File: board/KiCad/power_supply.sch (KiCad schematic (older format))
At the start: 8 parts, among them CON1 BARREL_JACK, Q1 IRLML6344bpf, U2 LD6815

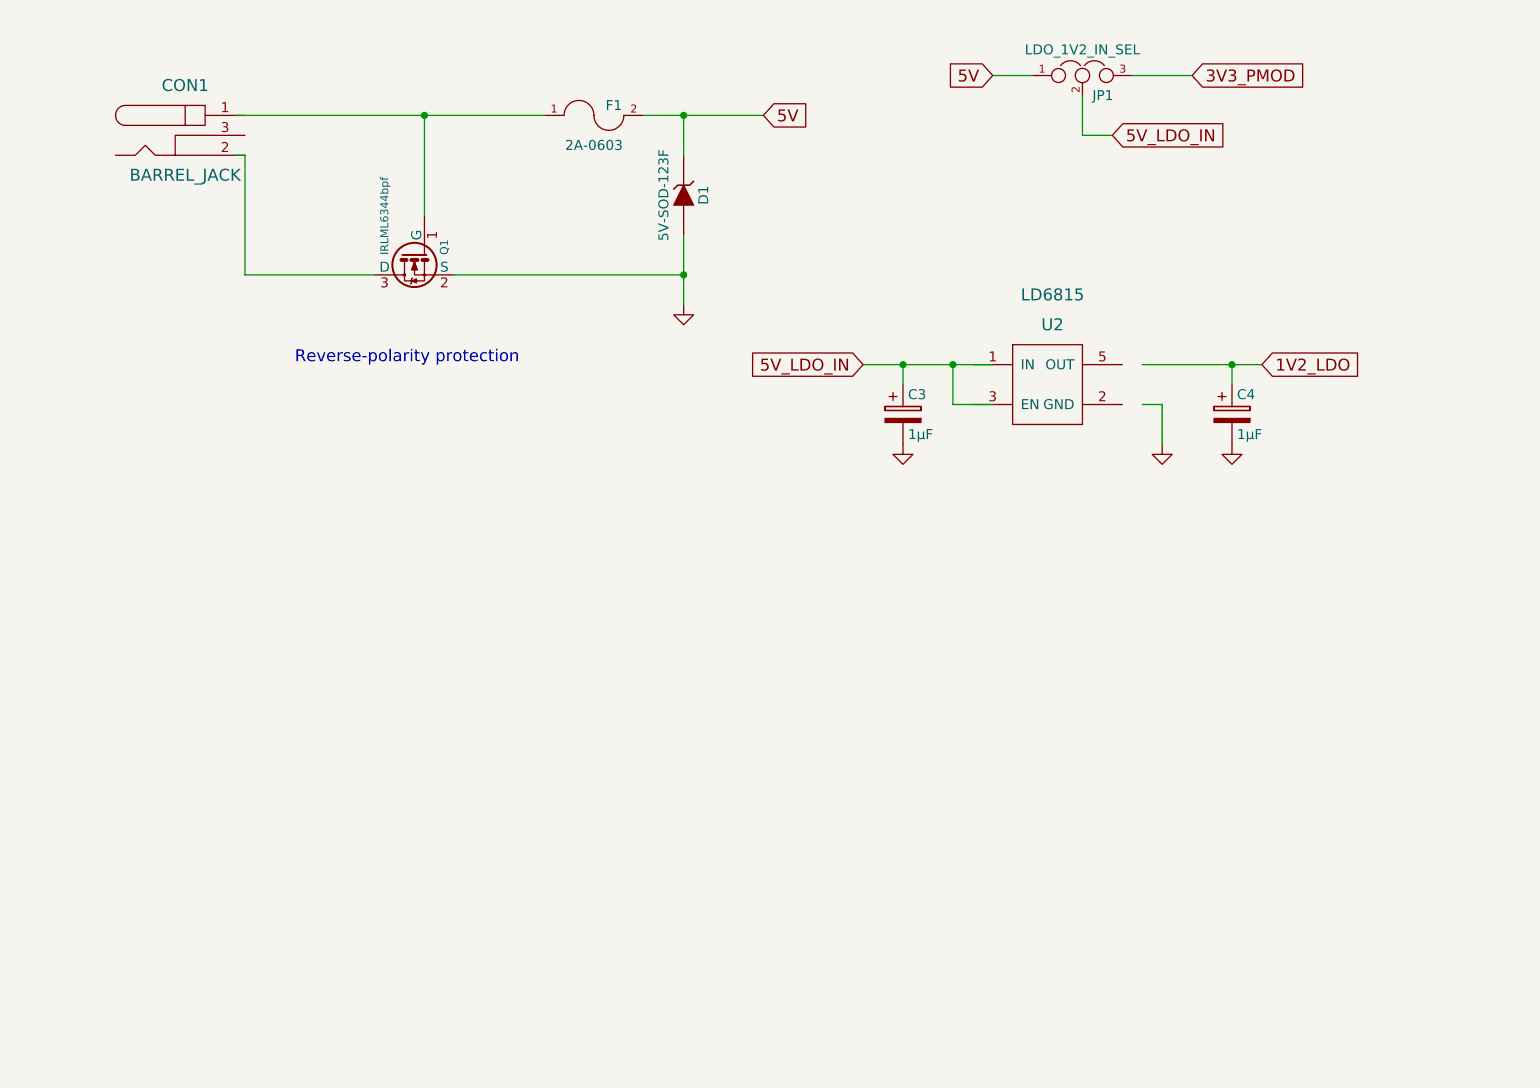
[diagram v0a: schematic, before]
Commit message: added annotations
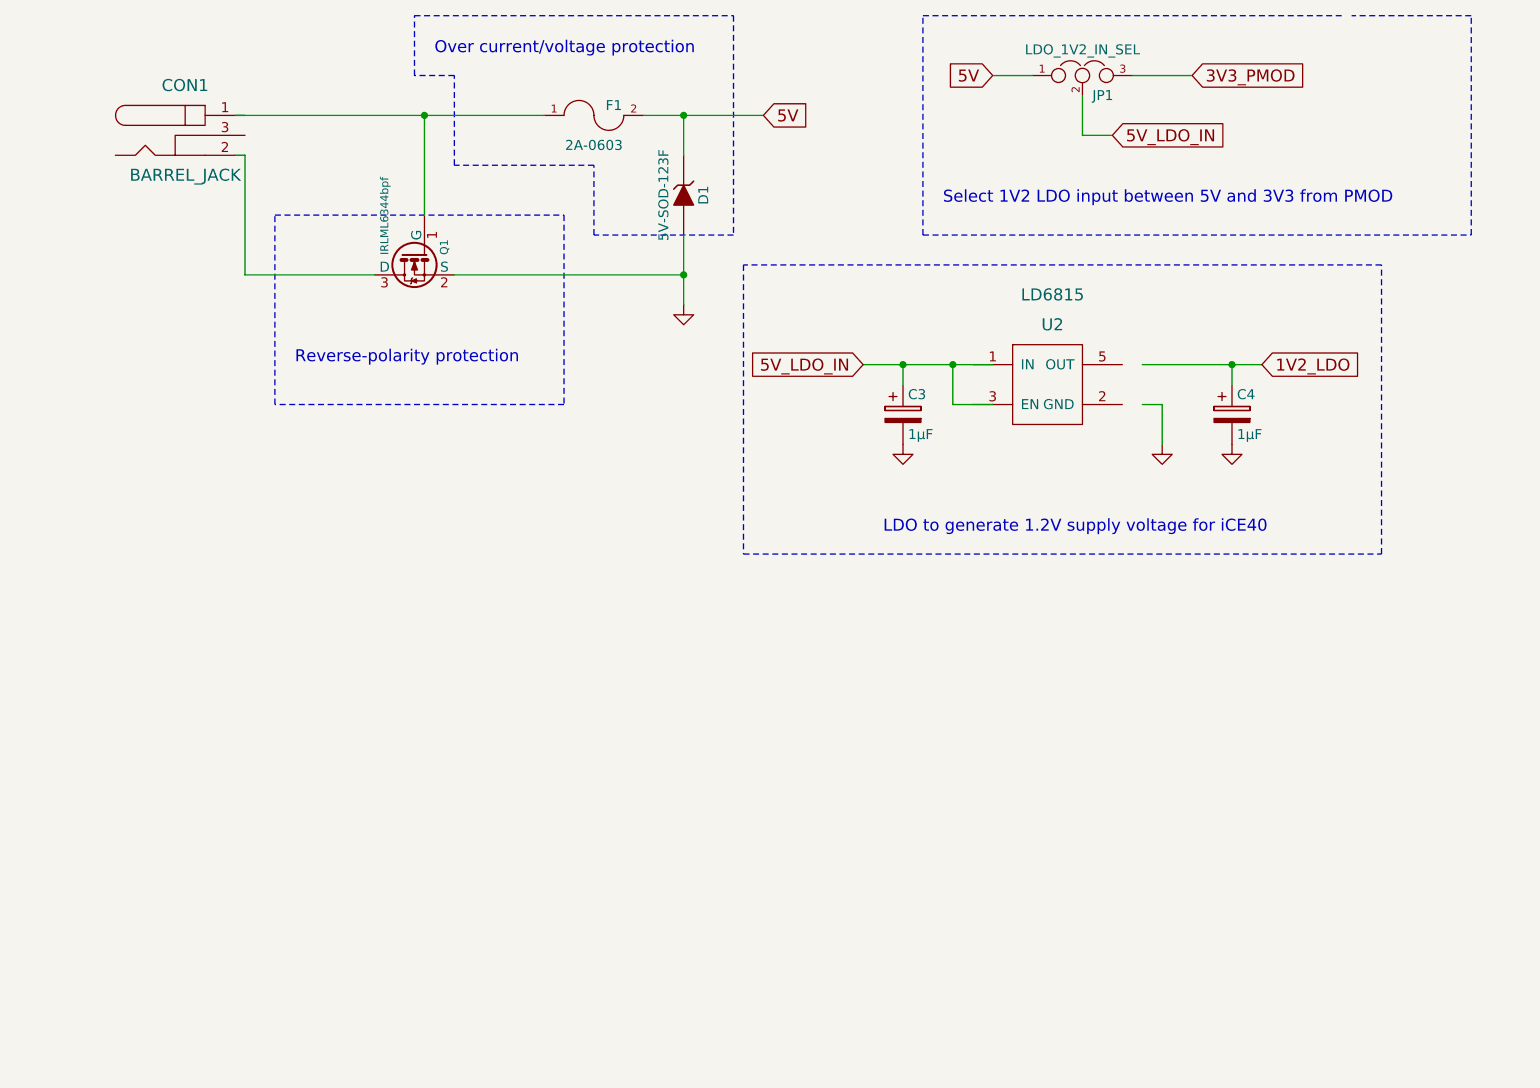
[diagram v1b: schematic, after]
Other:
- note added: "LDO to generate 1.2V supply voltage for iCE40"
- note added: "Over current/voltage protection"
- note added: "Select 1V2 LDO input between 5V and 3V3 from PMOD"
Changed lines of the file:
@@
 	4600 2300 4600 2650
 Connection ~ 4600 2500
+Wire Notes Line
+	2550 3150 2550 2200
+Wire Notes Line
+	2550 2200 4000 2200
+Wire Notes Line
+	4000 2200 4000 3150
+Wire Notes Line
+	4000 3150 2550 3150
+Text Notes 3350 1400 0    60   ~ 0
+Over current/voltage protection
+Wire Notes Line
+	3250 1200 4850 1200
+Wire Notes Line
+	4850 1200 4850 2300
+Wire Notes Line
+	4850 2300 4150 2300
+Wire Notes Line
+	4150 2300 4150 1950
+Wire Notes Line
+	4150 1950 3450 1950
+Wire Notes Line
+	3450 1950 3450 1500
+Wire Notes Line
+	3450 1500 3250 1500
+Wire Notes Line
+	3250 1500 3250 1200
+Wire Notes Line
+	5800 1200 7900 1200
+Wire Notes Line
+	5800 2300 8550 2300
+Wire Notes Line
+	5800 2300 5800 1200
+Text Notes 5900 2150 0    60   ~ 0
+Select 1V2 LDO input between 5V and 3V3 from PMOD
+Wire Notes Line
+	8550 2300 8550 1200
+Wire Notes Line
+	8550 1200 7950 1200
+Text Notes 5600 3800 0    60   ~ 0
+LDO to generate 1.2V supply voltage for iCE40
+Wire Notes Line
+	4900 2450 4900 3900
+Wire Notes Line
+	4900 3900 8100 3900
+Wire Notes Line
+	8100 3900 8100 2450
+Wire Notes Line
+	8100 2450 4900 2450
 $EndSCHEMATC

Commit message: SPI & Osci
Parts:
- added C?: 0.1µ, symbol C
- added J?: SELECT_DIV, Pinhead_1x3_TH, symbol Pinheader_1x3_TH
- added R?: R, symbol R
- added U?: LTC1799, symbol LTC1799
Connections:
- net labels added: ICE_CLK_IN
- wire segments 21 -> 34
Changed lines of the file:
@@
 $Descr A4 11693 8268
 encoding utf-8
-Sheet 5 5
+Sheet 5 6
 Title ""
 Date ""
@@
 Wire Notes Line
 	8100 2450 4900 2450
+$Comp
+L LTC1799 U?
+U 1 1 56BD2D04
+P 3450 6100
+F 0 "U?" H 3450 6100 60  0000 C CNN
+F 1 "LTC1799" H 3450 7100 60  0000 C CNN
+F 2 "" H 3450 6100 60  0000 C CNN
+F 3 "" H 3450 6100 60  0000 C CNN
+	1    3450 6100
+	1    0    0    -1
+$EndComp
+Text GLabel 2000 5350 0    60   Input ~ 0
+3V3_PMOD
+$Comp
+L C C?
+U 1 1 56BD346E
+P 2200 5600
+F 0 "C?" H 2225 5700 50  0000 L CNN
+F 1 "0.1µ" H 2225 5500 50  0000 L CNN
+F 2 "" H 2238 5450 30  0000 C CNN
+F 3 "" H 2200 5600 60  0000 C CNN
+	1    2200 5600
+	1    0    0    -1
+$EndComp
+$Comp
+L GND #PWR?
+U 1 1 56BD34C1
+P 2200 6100
+F 0 "#PWR?" H 2200 5850 50  0001 C CNN
+F 1 "GND" H 2200 5950 50  0000 C CNN
+F 2 "" H 2200 6100 60  0000 C CNN
+F 3 "" H 2200 6100 60  0000 C CNN
+	1    2200 6100
+	1    0    0    -1
+$EndComp
+Wire Wire Line
+	2000 5350 3000 5350
+Wire Wire Line
+	2200 5450 2200 5350
+Connection ~ 2200 5350
+Wire Wire Line
+	2200 5750 2200 6100
+$Comp
+L R R?
+U 1 1 56BD37E8
+P 2650 5600
+F 0 "R?" V 2730 5600 50  0000 C CNN
+F 1 "R" V 2650 5600 50  0000 C CNN
+F 2 "" V 2580 5600 30  0000 C CNN
+F 3 "" H 2650 5600 30  0000 C CNN
+	1    2650 5600
+	0    1    1    0
+$EndComp
+Wire Wire Line
+	2800 5600 3000 5600
+Wire Wire Line
+	2500 5350 2500 5600
+Connection ~ 2500 5350
+Wire Wire Line
+	3000 5850 2200 5850
+Connection ~ 2200 5850
+$Comp
+L Pinheader_1x3_TH J?
+U 1 1 56BD3EF9
+P 4400 5800
+F 0 "J?" H 4400 6050 60  0000 C CNN
+F 1 "SELECT_DIV" H 4400 6190 60  0001 C CNN
+F 2 "Pinhead_1x3_TH" H 4390 6300 60  0001 C CNN
+F 3 "" H 4400 5800 60  0000 C CNN
+F 4 "609-3461-ND" H 4380 6820 60  0001 C CNN "Vendor Part Number"
+F 5 "68000-103HLF" H 4370 6530 60  0001 C CNN "Manufacturer Part Number"
+F 6 "BERGSTIK II, .100\", SR, STRAIGHT," H 4350 6410 60  0001 C CNN "Description"
+F 7 "Digi-Key" H 4370 6730 60  0001 C CNN "Vendor"
+F 8 "FCI" H 4360 6620 60  0001 C CNN "Manufacturer"
+F 9 "PinH_1x3_TH" H 4410 5650 60  0000 C CNN "Component Value"
+	1    4400 5800
+	-1   0    0    1
+$EndComp
+Wire Wire Line
+	3900 5850 4150 5850
+$Comp
+L GND #PWR?
+U 1 1 56BD3FC7
+P 4100 6050
+F 0 "#PWR?" H 4100 5800 50  0001 C CNN
+F 1 "GND" H 4100 5900 50  0000 C CNN
+F 2 "" H 4100 6050 60  0000 C CNN
+F 3 "" H 4100 6050 60  0000 C CNN
+	1    4100 6050
+	1    0    0    -1
+$EndComp
+Wire Wire Line
+	4100 6050 4100 5950
+Wire Wire Line
+	4100 5950 4150 5950
+Text GLabel 4250 5550 2    60   Input ~ 0
+3V3_PMOD
+Wire Wire Line
+	4150 5750 4000 5750
+Wire Wire Line
+	4000 5750 4000 5550
+Wire Wire Line
+	4000 5550 4250 5550
+Text GLabel 4250 5350 2    60   Input ~ 0
+ICE_CLK_IN
+Wire Wire Line
+	3900 5350 4250 5350
 $EndSCHEMATC

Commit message: minor changes
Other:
- note added: "Clock generation"
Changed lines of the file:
@@
 $EndComp
 Text GLabel 2000 5350 0    60   Input ~ 0
-3V3_PMOD
+5V_LDO_IN
 $Comp
 L C C?
@@
 	4100 5950 4150 5950
 Text GLabel 4250 5550 2    60   Input ~ 0
-3V3_PMOD
+5V_LDO_IN
 Wire Wire Line
 	4150 5750 4000 5750
@@
 Wire Wire Line
 	3900 5350 4250 5350
+Wire Notes Line
+	1250 4900 5100 4900
+Wire Notes Line
+	5100 4900 5100 6500
+Wire Notes Line
+	5100 6500 1250 6500
+Wire Notes Line
+	1250 6500 1250 4900
+Text Notes 2750 6400 0    60   ~ 0
+Clock generation
 $EndSCHEMATC

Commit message: Finalize first draft
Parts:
- C3, C4: footprint (none) -> Capacitors_Tantalum_SMD:TantalC_SizeA_EIA-3216_HandSoldering
- C5: renamed from C?; footprint (none) -> Capacitors_SMD:C_0603_HandSoldering
- CON1: footprint (none) -> Connect:BARREL_JACK
- D1: footprint (none) -> pmod:SOD-123F_Handsoldering
- F1: footprint (none) -> Capacitors_SMD:C_0603_HandSoldering
- J3: renamed from J?; footprint Pinhead_1x3_TH -> Pin_Headers:Pin_Header_Straight_1x03
- JP1: footprint (none) -> Pin_Headers:Pin_Header_Straight_1x03
- Q1: footprint (none) -> TO_SOT_Packages_SMD:SOT-23_Handsoldering
- R5: renamed from R?; footprint (none) -> Resistors_SMD:R_0603_HandSoldering
- U2: footprint (none) -> pmod:SOT-753_(TSOP-5)_Handsoldering
- U3: renamed from U?; footprint (none) -> pmod:TSOT-23_Handsoldering
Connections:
- wire segments 34 -> 35
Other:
- moved on the sheet: U2
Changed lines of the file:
@@
 F 0 "Q1" H 3250 2251 40  0000 R CNN
 F 1 "IRLML6344bpf" H 3250 2550 40  0000 R CNN
-F 2 "" H 3120 2502 29  0000 C CNN
+F 2 "TO_SOT_Packages_SMD:SOT-23_Handsoldering" H 3120 2502 29  0001 C CNN
 F 3 "" H 3250 2400 60  0000 C CNN
 	1    3250 2400
@@
 $EndComp
 Wire Wire Line
-	2350 1700 3900 1700
-Wire Wire Line
 	3300 1700 3300 2200
-Wire Wire Line
-	2350 1900 2400 1900
-Wire Wire Line
-	2400 1900 2400 2500
-Wire Wire Line
-	2400 2500 3050 2500
 Wire Wire Line
 	3450 2500 4600 2500
 Connection ~ 3300 1700
 $Comp
-L GND #PWR14
+L GND #PWR15
 U 1 1 56A748C9
 P 4600 2650
-F 0 "#PWR14" H 4600 2650 30  0001 C CNN
+F 0 "#PWR15" H 4600 2650 30  0001 C CNN
 F 1 "GND" H 4600 2580 30  0001 C CNN
 F 2 "" H 4600 2650 60  0000 C CNN
@@
 F 0 "CON1" H 2100 2050 60  0000 C CNN
 F 1 "BARREL_JACK" H 2100 1600 60  0000 C CNN
-F 2 "" H 2100 1800 60  0001 C CNN
+F 2 "Connect:BARREL_JACK" H 2100 1800 60  0001 C CNN
 F 3 "" H 2100 1800 60  0000 C CNN
 	1    2100 1800
@@
 L LD6815 U2
 U 1 1 56AB720B
-P 6450 2750
-F 0 "U2" H 6450 2750 60  0000 C CNN
-F 1 "LD6815" H 6450 2900 60  0000 C CNN
-F 2 "" H 6450 2750 60  0001 C CNN
-F 3 "" H 6450 2750 60  0000 C CNN
-	1    6450 2750
+P 6550 2750
+F 0 "U2" H 6550 2750 60  0000 C CNN
+F 1 "LD6815" H 6550 2900 60  0000 C CNN
+F 2 "pmod:SOT-753_(TSOP-5)_Handsoldering" H 6550 2750 60  0001 C CNN
+F 3 "" H 6550 2750 60  0000 C CNN
+	1    6550 2750
 	1    0    0    -1
 $EndComp
@@
 	6900 2950 7500 2950
 $Comp
-L GND #PWR16
+L GND #PWR27
 U 1 1 56AB761D
 P 7000 3350
-F 0 "#PWR16" H 7000 3350 30  0001 C CNN
+F 0 "#PWR27" H 7000 3350 30  0001 C CNN
 F 1 "GND" H 7000 3280 30  0001 C CNN
 F 2 "" H 7000 3350 60  0000 C CNN
@@
 F 0 "JP1" H 6650 1400 50  0000 L CNN
 F 1 "LDO_1V2_IN_SEL" H 6600 1600 50  0000 C BNN
-F 2 "" H 6600 1500 60  0001 C CNN
+F 2 "Pin_Headers:Pin_Header_Straight_1x03" H 6600 1500 60  0001 C CNN
 F 3 "" H 6600 1500 60  0000 C CNN
 	1    6600 1500
@@
 F 0 "C4" H 7375 3300 50  0000 L CNN
 F 1 "1µF" H 7375 3100 50  0000 L CNN
-F 2 "" H 7388 3050 30  0001 C CNN
+F 2 "Capacitors_Tantalum_SMD:TantalC_SizeA_EIA-3216_HandSoldering" H 7388 3050 30  0001 C CNN
 F 3 "" H 7350 3200 60  0000 C CNN
 	1    7350 3200
@@
 F 0 "C3" H 5725 3300 50  0000 L CNN
 F 1 "1µF" H 5725 3100 50  0000 L CNN
-F 2 "" H 5738 3050 30  0001 C CNN
+F 2 "Capacitors_Tantalum_SMD:TantalC_SizeA_EIA-3216_HandSoldering" H 5738 3050 30  0001 C CNN
 F 3 "" H 5700 3200 60  0000 C CNN
 	1    5700 3200
@@
 Connection ~ 7350 2950
 $Comp
-L GND #PWR17
+L GND #PWR29
 U 1 1 56AB861C
 P 7350 3350
-F 0 "#PWR17" H 7350 3350 30  0001 C CNN
+F 0 "#PWR29" H 7350 3350 30  0001 C CNN
 F 1 "GND" H 7350 3280 30  0001 C CNN
 F 2 "" H 7350 3350 60  0000 C CNN
@@
 $EndComp
 $Comp
-L GND #PWR15
+L GND #PWR24
 U 1 1 56AB8639
 P 5700 3350
-F 0 "#PWR15" H 5700 3350 30  0001 C CNN
+F 0 "#PWR24" H 5700 3350 30  0001 C CNN
 F 1 "GND" H 5700 3280 30  0001 C CNN
 F 2 "" H 5700 3350 60  0000 C CNN
@@
 F 0 "F1" H 4250 1750 50  0000 C CNN
 F 1 "2A-0603" H 4150 1550 50  0000 C CNN
-F 2 "" H 4150 1700 50  0001 C CNN
+F 2 "Capacitors_SMD:C_0603_HandSoldering" H 4150 1700 50  0001 C CNN
 F 3 "" H 4150 1700 50  0000 C CNN
 	1    4150 1700
@@
 F 0 "D1" H 4600 2200 50  0000 C CNN
 F 1 "5V-SOD-123F" H 4600 2000 50  0000 C CNN
-F 2 "" H 4600 2100 50  0001 C CNN
+F 2 "pmod:SOD-123F_Handsoldering" H 4600 2100 50  0001 C CNN
 F 3 "" H 4600 2100 50  0000 C CNN
 	1    4600 2100
@@
 	8100 2450 4900 2450
 $Comp
-L LTC1799 U?
+L LTC1799 U3
 U 1 1 56BD2D04
 P 3450 6100
-F 0 "U?" H 3450 6100 60  0000 C CNN
+F 0 "U3" H 3450 6100 60  0000 C CNN
 F 1 "LTC1799" H 3450 7100 60  0000 C CNN
-F 2 "" H 3450 6100 60  0000 C CNN
+F 2 "pmod:TSOT-23_Handsoldering" H 3450 6100 60  0001 C CNN
 F 3 "" H 3450 6100 60  0000 C CNN
 	1    3450 6100
@@
 5V_LDO_IN
 $Comp
-L C C?
+L C C5
 U 1 1 56BD346E
 P 2200 5600
-F 0 "C?" H 2225 5700 50  0000 L CNN
+F 0 "C5" H 2225 5700 50  0000 L CNN
 F 1 "0.1µ" H 2225 5500 50  0000 L CNN
-F 2 "" H 2238 5450 30  0000 C CNN
+F 2 "Capacitors_SMD:C_0603_HandSoldering" H 2238 5450 30  0001 C CNN
 F 3 "" H 2200 5600 60  0000 C CNN
 	1    2200 5600
@@
 $EndComp
 $Comp
-L GND #PWR?
+L GND #PWR3
 U 1 1 56BD34C1
 P 2200 6100
-F 0 "#PWR?" H 2200 5850 50  0001 C CNN
+F 0 "#PWR3" H 2200 5850 50  0001 C CNN
 F 1 "GND" H 2200 5950 50  0000 C CNN
 F 2 "" H 2200 6100 60  0000 C CNN
@@
 	2200 5750 2200 6100
 $Comp
-L R R?
+L R R5
 U 1 1 56BD37E8
 P 2650 5600
-F 0 "R?" V 2730 5600 50  0000 C CNN
+F 0 "R5" V 2730 5600 50  0000 C CNN
 F 1 "R" V 2650 5600 50  0000 C CNN
-F 2 "" V 2580 5600 30  0000 C CNN
+F 2 "Resistors_SMD:R_0603_HandSoldering" V 2580 5600 30  0001 C CNN
 F 3 "" H 2650 5600 30  0000 C CNN
 	1    2650 5600
@@
 Connection ~ 2200 5850
 $Comp
-L Pinheader_1x3_TH J?
+L Pinheader_1x3_TH J3
 U 1 1 56BD3EF9
 P 4400 5800
-F 0 "J?" H 4400 6050 60  0000 C CNN
+F 0 "J3" H 4400 6050 60  0000 C CNN
 F 1 "SELECT_DIV" H 4400 6190 60  0001 C CNN
-F 2 "Pinhead_1x3_TH" H 4390 6300 60  0001 C CNN
+F 2 "Pin_Headers:Pin_Header_Straight_1x03" H 4390 6300 60  0001 C CNN
 F 3 "" H 4400 5800 60  0000 C CNN
 F 4 "609-3461-ND" H 4380 6820 60  0001 C CNN "Vendor Part Number"
@@
 	3900 5850 4150 5850
 $Comp
-L GND #PWR?
+L GND #PWR12
 U 1 1 56BD3FC7
 P 4100 6050
-F 0 "#PWR?" H 4100 5800 50  0001 C CNN
+F 0 "#PWR12" H 4100 5800 50  0001 C CNN
 F 1 "GND" H 4100 5900 50  0000 C CNN
 F 2 "" H 4100 6050 60  0000 C CNN
@@
 Text Notes 2750 6400 0    60   ~ 0
 Clock generation
+Wire Wire Line
+	2400 1800 2450 1800
+Wire Wire Line
+	2450 1800 2450 2500
+Wire Wire Line
+	2450 1900 2400 1900
+Wire Wire Line
+	2450 2500 3050 2500
+Connection ~ 2450 1900
+Wire Wire Line
+	3900 1700 2400 1700
 $EndSCHEMATC

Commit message: Improve design
* PMOS on input voltage for polarity
* Re-design board to add mount holes and better routing
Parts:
- removed Q1: IRLML6344bpf, TO_SOT_Packages_SMD:SOT-23_Handsoldering, symbol BSS138
- added Q1: Q_PMOS_GSD, TO_SOT_Packages_SMD:SOT-23_Handsoldering, symbol Q_PMOS_GSD
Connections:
- net labels added: VIN, VIN_PROT
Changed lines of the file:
@@
 Comment4 ""
 $EndDescr
-$Comp
-L BSS138 Q1
-U 1 1 56A747AC
-P 3250 2400
-F 0 "Q1" H 3250 2251 40  0000 R CNN
-F 1 "IRLML6344bpf" H 3250 2550 40  0000 R CNN
-F 2 "TO_SOT_Packages_SMD:SOT-23_Handsoldering" H 3120 2502 29  0001 C CNN
-F 3 "" H 3250 2400 60  0000 C CNN
-	1    3250 2400
-	0    -1   1    0
-$EndComp
-Wire Wire Line
-	3300 1700 3300 2200
-Wire Wire Line
-	3450 2500 4600 2500
-Connection ~ 3300 1700
-$Comp
-L GND #PWR15
+Wire Wire Line
+	2450 2500 4600 2500
+$Comp
+L GND #PWR32
 U 1 1 56A748C9
 P 4600 2650
-F 0 "#PWR15" H 4600 2650 30  0001 C CNN
+F 0 "#PWR32" H 4600 2650 30  0001 C CNN
 F 1 "GND" H 4600 2580 30  0001 C CNN
 F 2 "" H 4600 2650 60  0000 C CNN
@@
 	6900 2950 7500 2950
 $Comp
-L GND #PWR27
+L GND #PWR34
 U 1 1 56AB761D
 P 7000 3350
-F 0 "#PWR27" H 7000 3350 30  0001 C CNN
+F 0 "#PWR34" H 7000 3350 30  0001 C CNN
 F 1 "GND" H 7000 3280 30  0001 C CNN
 F 2 "" H 7000 3350 60  0000 C CNN
@@
 Connection ~ 7350 2950
 $Comp
-L GND #PWR29
+L GND #PWR35
 U 1 1 56AB861C
 P 7350 3350
-F 0 "#PWR29" H 7350 3350 30  0001 C CNN
+F 0 "#PWR35" H 7350 3350 30  0001 C CNN
 F 1 "GND" H 7350 3280 30  0001 C CNN
 F 2 "" H 7350 3350 60  0000 C CNN
@@
 $EndComp
 $Comp
-L GND #PWR24
+L GND #PWR33
 U 1 1 56AB8639
 P 5700 3350
-F 0 "#PWR24" H 5700 3350 30  0001 C CNN
+F 0 "#PWR33" H 5700 3350 30  0001 C CNN
 F 1 "GND" H 5700 3280 30  0001 C CNN
 F 2 "" H 5700 3350 60  0000 C CNN
@@
 	1    0    0    -1
 $EndComp
-Text Notes 2650 2950 0    60   ~ 0
+Text Notes 1900 1350 0    60   ~ 0
 Reverse-polarity protection
 $Comp
@@
 	4600 2300 4600 2650
 Connection ~ 4600 2500
-Wire Notes Line
-	2550 3150 2550 2200
-Wire Notes Line
-	2550 2200 4000 2200
-Wire Notes Line
-	4000 2200 4000 3150
-Wire Notes Line
-	4000 3150 2550 3150
 Text Notes 3350 1400 0    60   ~ 0
 Over current/voltage protection
@@
 $EndComp
 $Comp
-L GND #PWR3
+L GND #PWR30
 U 1 1 56BD34C1
 P 2200 6100
-F 0 "#PWR3" H 2200 5850 50  0001 C CNN
+F 0 "#PWR30" H 2200 5850 50  0001 C CNN
 F 1 "GND" H 2200 5950 50  0000 C CNN
 F 2 "" H 2200 6100 60  0000 C CNN
@@
 	3900 5850 4150 5850
 $Comp
-L GND #PWR12
+L GND #PWR31
 U 1 1 56BD3FC7
 P 4100 6050
-F 0 "#PWR12" H 4100 5800 50  0001 C CNN
+F 0 "#PWR31" H 4100 5800 50  0001 C CNN
 F 1 "GND" H 4100 5900 50  0000 C CNN
 F 2 "" H 4100 6050 60  0000 C CNN
@@
 Wire Wire Line
 	2450 1900 2400 1900
-Wire Wire Line
-	2450 2500 3050 2500
 Connection ~ 2450 1900
-Wire Wire Line
-	3900 1700 2400 1700
+$Comp
+L Q_PMOS_GSD Q1
+U 1 1 56C43C16
+P 2900 1800
+F 0 "Q1" V 3232 1800 50  0000 C CNN
+F 1 "Q_PMOS_GSD" V 3140 1800 50  0000 C CNN
+F 2 "TO_SOT_Packages_SMD:SOT-23_Handsoldering" H 3100 1900 50  0001 C CNN
+F 3 "" H 2900 1800 50  0000 C CNN
+	1    2900 1800
+	0    -1   -1   0
+$EndComp
+Wire Notes Line
+	2600 1400 3200 1400
+Wire Notes Line
+	3200 1400 3200 2100
+Wire Notes Line
+	3200 2100 2600 2100
+Wire Notes Line
+	2600 2100 2600 1400
+Wire Wire Line
+	2400 1700 2700 1700
+Wire Wire Line
+	3100 1700 3900 1700
+Wire Wire Line
+	2900 2000 2900 2500
+Connection ~ 2900 2500
+Text Label 2450 1700 0    60   ~ 0
+VIN
+Text Label 3250 1700 0    60   ~ 0
+VIN_PROT
 $EndSCHEMATC
